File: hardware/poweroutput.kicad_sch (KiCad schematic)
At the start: 17 parts, among them J4 DG142R-5.08-02P-14-00AH, J5 108-0902-001, J6 108-0903-001, Q5 60V 4mR TBD, Q6 60V 4mR TBD, U12 AP74502Q

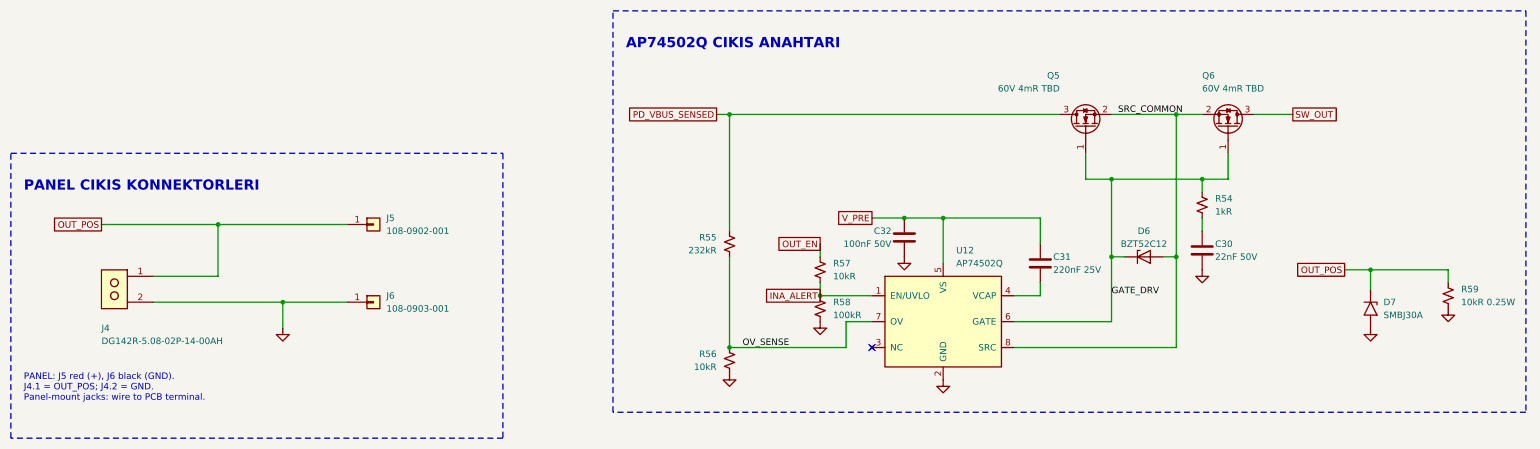
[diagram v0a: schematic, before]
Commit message: usb_pd_controller: VBUS dağıtımını tek sayfada topla (A2)
AP33772S bloğu ile VBUS şönt / PD çıkış anahtarı tek çerçevede birleşti:
USB_VBUS -> TP1 -> R11 şönt -> PD_VBUS_SENSED rayı -> Q4/Q3 -> PD_VOUT,
rayın devamı doğrudan AP74502Q bloğuna gidiyor. ISENP, VCC, PWR_EN->R12
kapı sürüşü ve VOUT geri beslemesi artık gerçek tellerle bağlı.

poweroutput'taki AP74502Q çıkış anahtarı ve powersensing'teki INA228
ölçüm bloğu bu sayfaya taşındı; SW_OUT ve PD_VBUS_SENSED sayfa içi yerel
etiket oldu (global etiketler kaldırıldı). poweroutput yalnızca panel
konnektörlerini tutuyor ve A4'e döndü; powersensing boşaldı.

Bağlantılar isimden bağımsız karşılaştırmayla doğrulandı: kayıp/yeni net
yok, yalnızca sayfa kapsamı değişen 5 net yeniden adlandı
(GATE_DRV, OV_SENSE, SRC_COMMON, PD_VBUS_SENSED, SW_OUT).
ERC değişmedi (0 hata, 2 eski uyarı).

Co-Authored-By: Claude Opus 5 <noreply@anthropic.com>
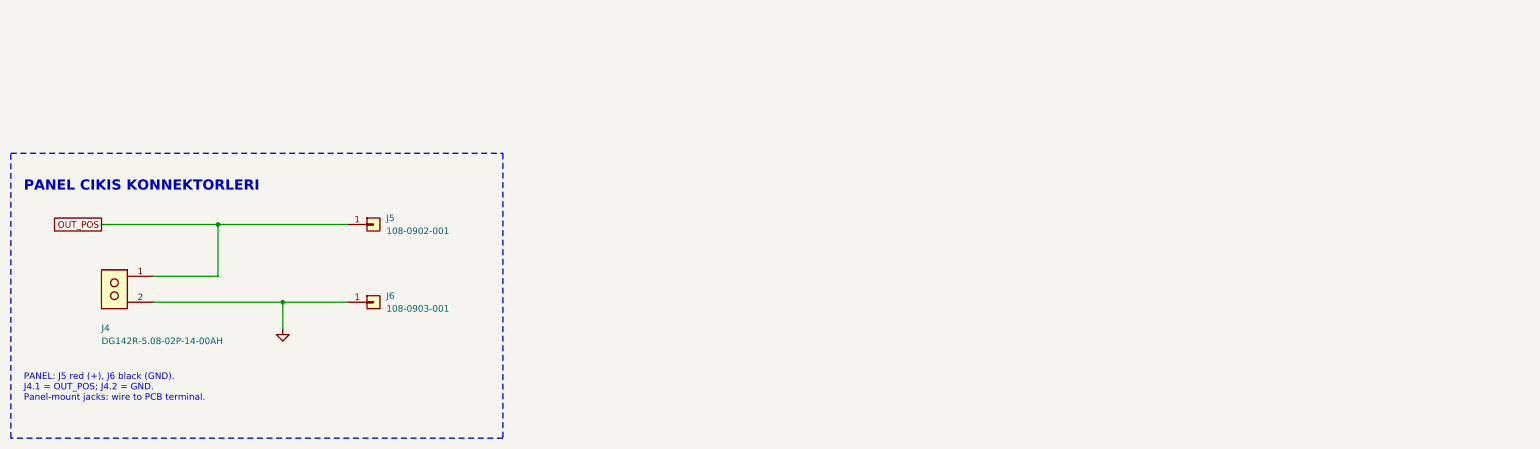
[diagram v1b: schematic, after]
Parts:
- removed C30: 22nF 50V, Capacitor_SMD:C_0402_1005Metric, symbol Device:C
- removed C31: 220nF 25V, Capacitor_SMD:C_0402_1005Metric, symbol Device:C
- removed C32: 100nF 50V, Capacitor_SMD:C_0402_1005Metric, symbol Device:C
- removed D6: BZT52C12, Diode_SMD:D_SOD-123, symbol Device:D_Zener
- removed D7: SMBJ30A, Diode_SMD:D_SMB, symbol Power_Path_Custom:SMBJ30A
- removed Q5, Q6: 60V 4mR TBD, symbol Transistor_FET:Q_NMOS_GSD
- removed R54: 1kR, Resistor_SMD:R_0402_1005Metric, symbol Device:R_Small_US
- removed R55: 232kR, Resistor_SMD:R_0402_1005Metric, symbol Device:R_Small_US
- removed R56, R57: 10kR, Resistor_SMD:R_0402_1005Metric, symbol Device:R_Small_US
- removed R58: 100kR, Resistor_SMD:R_0402_1005Metric, symbol Device:R_Small_US
- removed R59: 10kR 0.25W, Resistor_SMD:R_0402_1005Metric, symbol Device:R_Small_US
- removed U12: AP74502Q, Package_TO_SOT_SMD:TSOT-23-8_HandSoldering, symbol Power_Path_Custom:AP74502Q
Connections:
- no-connect marks 1 -> 0
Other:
- note removed: "AP74502Q CIKIS ANAHTARI"
